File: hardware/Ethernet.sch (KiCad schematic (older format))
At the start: 29 parts, among them J2 RJ45-TRANSFO, U3 DP83848C, X1 50Mhz

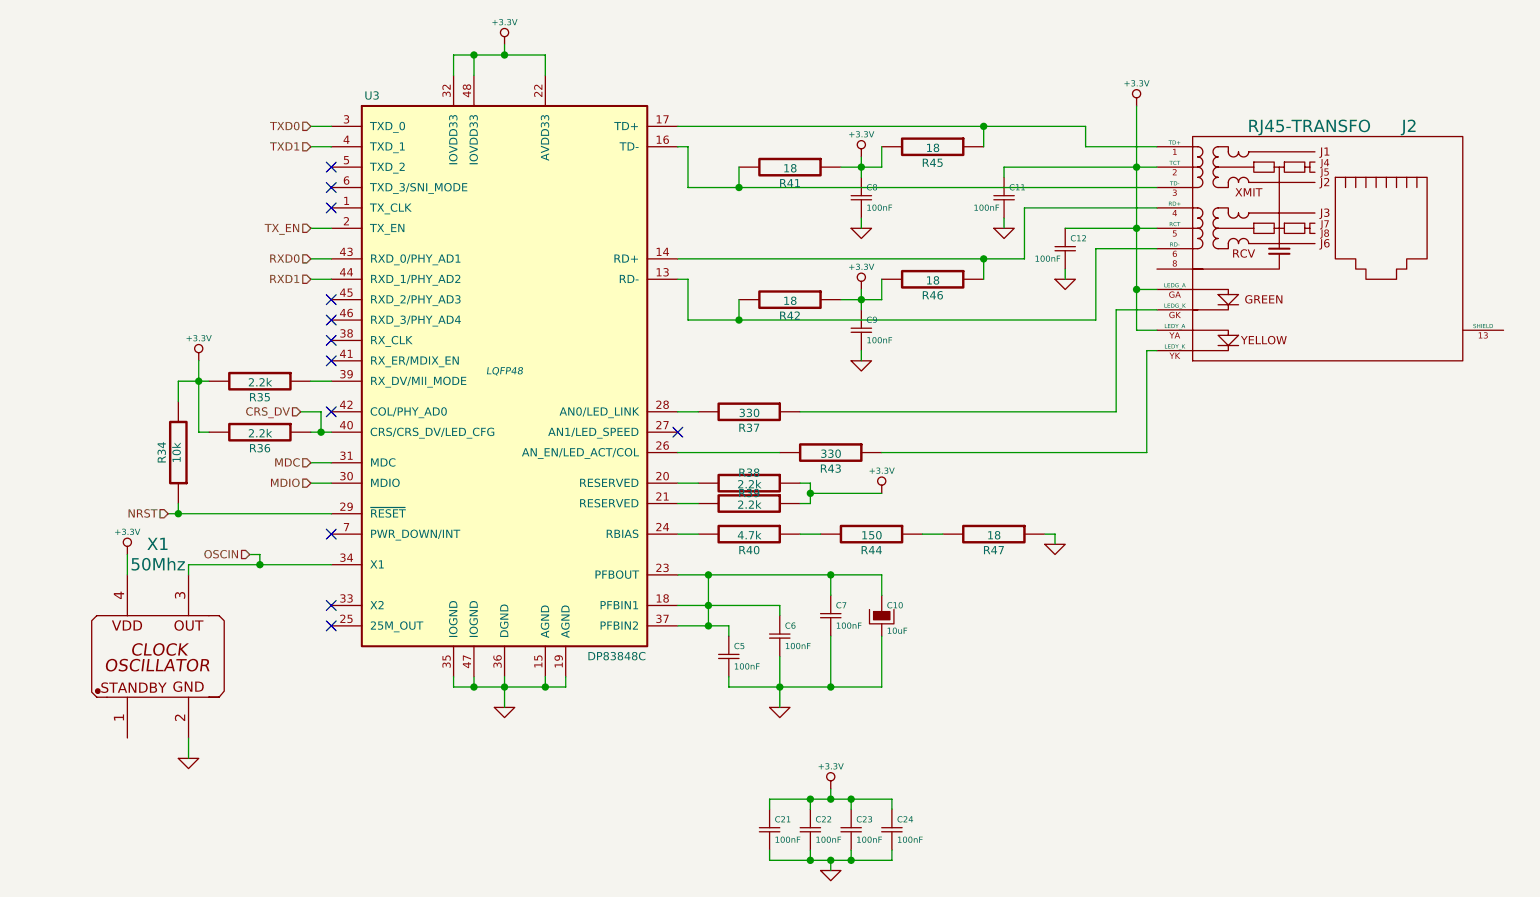
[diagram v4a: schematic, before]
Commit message: Terminado el Routeo de la Placa
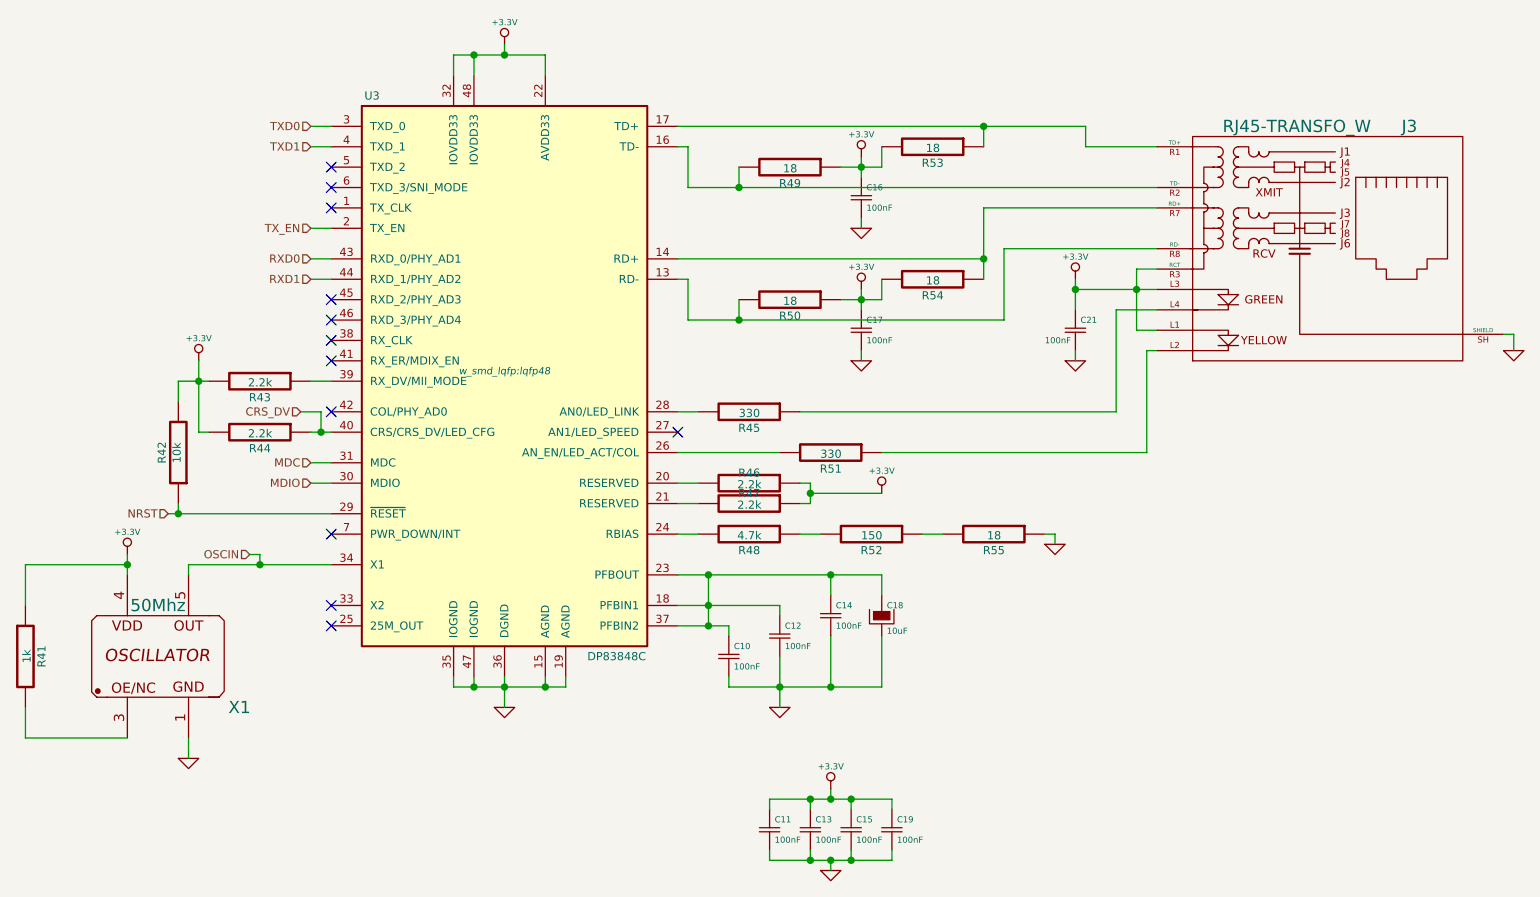
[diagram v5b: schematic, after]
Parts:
- removed C11: 100nF, Capacitors_SMD:c_1206, symbol Csmall
- removed J2: RJ45-TRANSFO, symbol RJ45-TRANSFO
- removed X1: 50Mhz, symbol OSCILLATOR-VDD-4
- added J3: RJ45-TRANSFO_W, w_Connectors:RJ45, symbol RJ45-TRANSFO_W
- added R41: 1k, Resistors_SMD:R_0805, symbol R
- added X1: 50Mhz, SMD_Packages:SOT-23-5, symbol OSCILLATOR-SOT23
- C10: renamed from C5; footprint Capacitors_SMD:c_1206 -> Capacitors_SMD:c_0805
- C11: renamed from C21; footprint Capacitors_SMD:c_1206 -> Capacitors_SMD:c_0805
- C12: renamed from C6; footprint Capacitors_SMD:c_1206 -> Capacitors_SMD:c_0805
- C13: renamed from C22; footprint Capacitors_SMD:c_1206 -> Capacitors_SMD:c_0805
- C14: renamed from C7; footprint Capacitors_SMD:c_1206 -> Capacitors_SMD:c_0805
- C15: renamed from C23; footprint Capacitors_SMD:c_1206 -> Capacitors_SMD:c_0805
- C16: renamed from C8; footprint Capacitors_SMD:c_1206 -> Capacitors_SMD:c_0805
- C17: renamed from C9; footprint Capacitors_SMD:c_1206 -> Capacitors_SMD:c_0805
- C19: renamed from C24; footprint Capacitors_SMD:c_1206 -> Capacitors_SMD:c_0805
- C21: renamed from C12; footprint Capacitors_SMD:c_1206 -> Capacitors_SMD:c_0805
- R42: renamed from R34; footprint Resistors_SMD:Resistor_SMD1206_ReflowWave -> Resistors_SMD:R_0805
- R43: renamed from R35; footprint Resistors_SMD:Resistor_SMD1206_ReflowWave -> Resistors_SMD:R_0805
- R44: renamed from R36; footprint Resistors_SMD:Resistor_SMD1206_ReflowWave -> Resistors_SMD:R_0805
- R45: renamed from R37; footprint Resistors_SMD:Resistor_SMD1206_ReflowWave -> Resistors_SMD:R_0805
- R46: renamed from R38; footprint Resistors_SMD:Resistor_SMD1206_ReflowWave -> Resistors_SMD:R_0805
- R47: renamed from R39; footprint Resistors_SMD:Resistor_SMD1206_ReflowWave -> Resistors_SMD:R_0805
- R48: renamed from R40; footprint Resistors_SMD:Resistor_SMD1206_ReflowWave -> Resistors_SMD:R_0805
- R49: renamed from R41; footprint Resistors_SMD:Resistor_SMD1206_ReflowWave -> Resistors_SMD:R_0805
- R50: renamed from R42; footprint Resistors_SMD:Resistor_SMD1206_ReflowWave -> Resistors_SMD:R_0805
- R51: renamed from R43; footprint Resistors_SMD:Resistor_SMD1206_ReflowWave -> Resistors_SMD:R_0805
- R52: renamed from R44; footprint Resistors_SMD:Resistor_SMD1206_ReflowWave -> Resistors_SMD:R_0805
- R53: renamed from R45; footprint Resistors_SMD:Resistor_SMD1206_ReflowWave -> Resistors_SMD:R_0805
- R54: renamed from R46; footprint Resistors_SMD:Resistor_SMD1206_ReflowWave -> Resistors_SMD:R_0805
- R55: renamed from R47; footprint Resistors_SMD:Resistor_SMD1206_ReflowWave -> Resistors_SMD:R_0805
- U3: footprint LQFP48 -> w_smd_lqfp:lqfp48
- renumbered C10 to C18
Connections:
- net +3.3V: now also J3.L1, J3.L3, J3.R3 (RCT), R41.1, X1.4 (VDD)
- net GND: now also J3.SH (SHIELD), X1.1 (GND)
- net OSCIN: now also X1.5 (OUT)
- net at R50.2, U3.13 (RD-): now also J3.R8 (RD-)
- net at R54.1, U3.14 (RD+): now also J3.R7 (RD+)
- net at R49.2, U3.16 (TD-): now also J3.R2 (TD-)
- net at R53.1, U3.17 (TD+): now also J3.R1 (TD+)
- net at R45.1: now also J3.L4
- net at R51.1: now also J3.L2
- new net: R41.2, X1.3 (STANDBY)
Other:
- moved on the sheet: C21

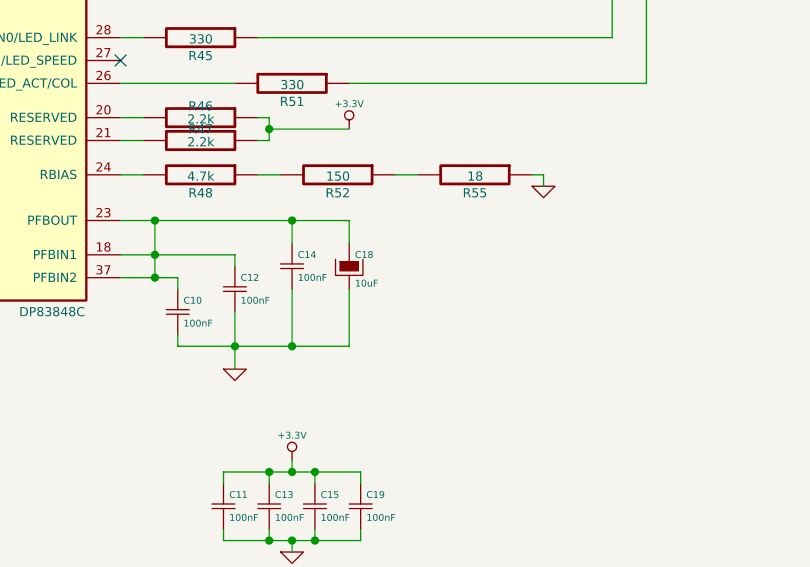
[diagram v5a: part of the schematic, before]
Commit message: Se reRouteo con clearance 12 en general
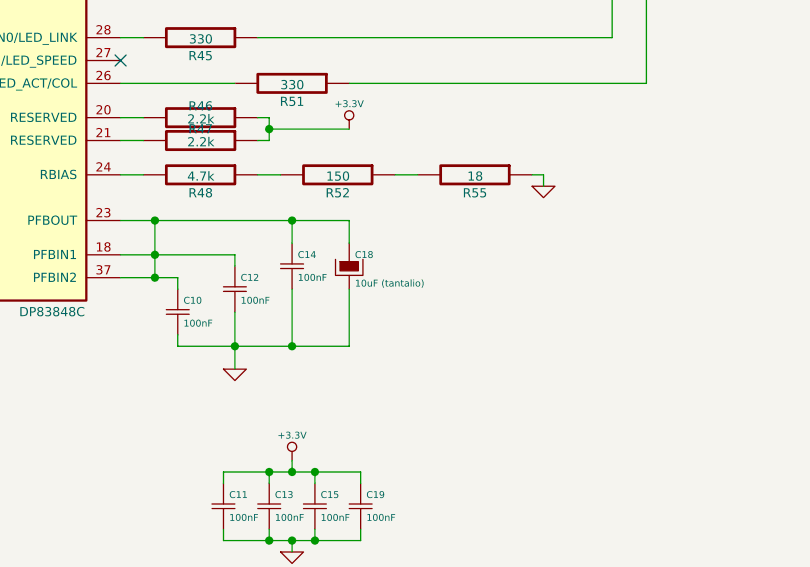
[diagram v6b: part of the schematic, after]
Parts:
- C18: value 10uF -> 10uF (tantalio); footprint Capacitors_ThroughHole:Capacitor5x11RM2.5 -> Capacitors_Tantalum_SMD:TantalC_SizeA_EIA-3216_HandSoldering
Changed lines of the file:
@@
 P 6350 4800
 F 0 "C18" H 6375 4850 30  0000 L CNN
-F 1 "10uF" H 6375 4725 30  0000 L CNN
-F 2 "Capacitors_ThroughHole:Capacitor5x11RM2.5" H 6350 4800 60  0001 C CNN
+F 1 "10uF (tantalio)" H 6375 4725 30  0000 L CNN
+F 2 "Capacitors_Tantalum_SMD:TantalC_SizeA_EIA-3216_HandSoldering" H 6350 4800 60  0001 C CNN
 F 3 "" H 6350 4800 60  0000 C CNN
 	1    6350 4800

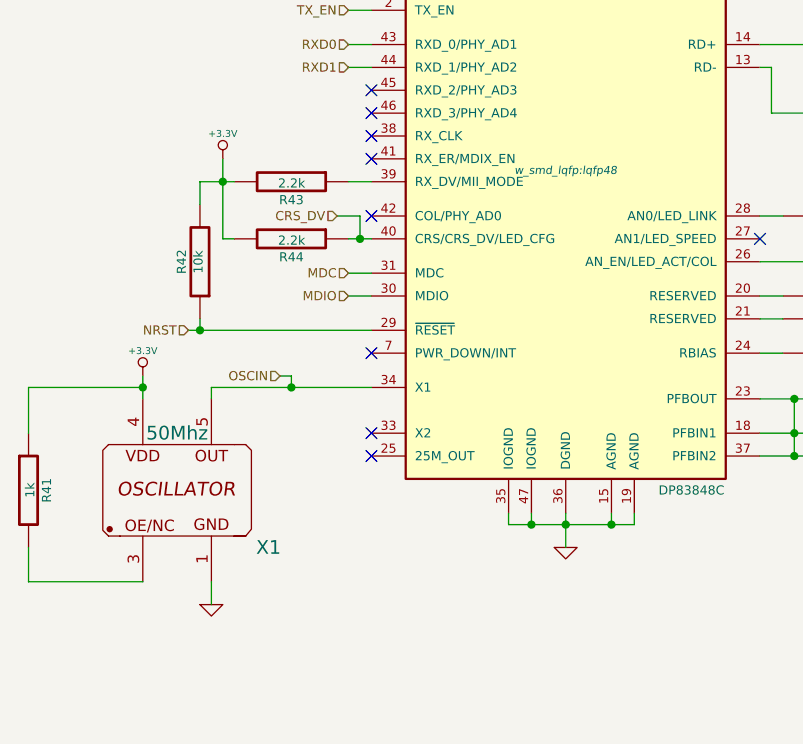
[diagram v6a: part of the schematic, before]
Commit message: Placa terminada, serigrafia verificada, logos agregados
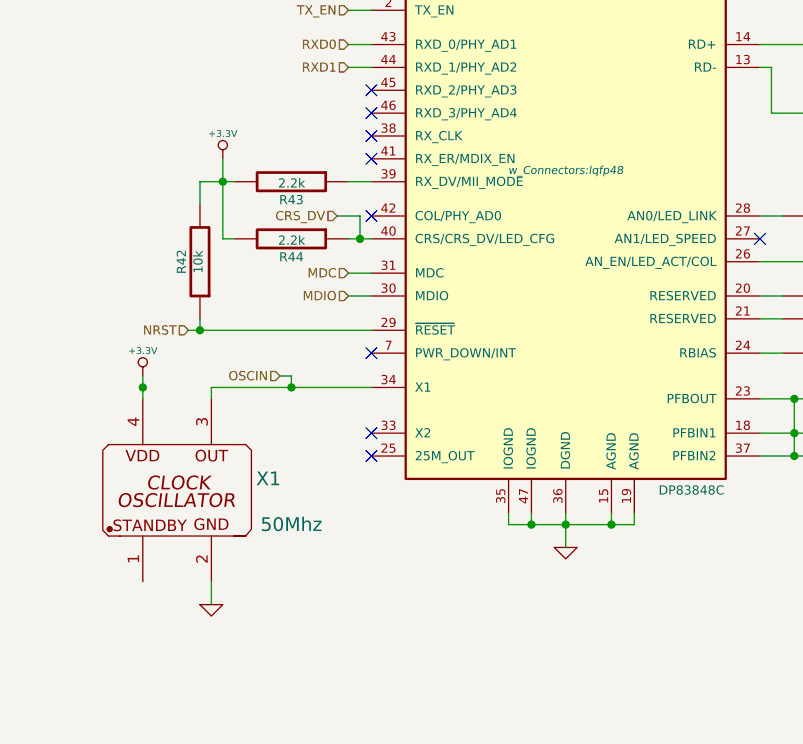
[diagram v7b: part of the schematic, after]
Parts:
- removed R41: 1k, Resistors_SMD:R_0805, symbol R
- removed X1: 50Mhz, SMD_Packages:SOT-23-5, symbol OSCILLATOR-SOT23
- added X1: 50Mhz, w_Connectors:crystal_fa128, symbol OSCILLATOR-VDD-4
- C10, C11, C12, C13, C14, C15, C16, C17, C19, C21: footprint Capacitors_SMD:c_0805 -> w_Connectors:c_0805
- U3: footprint w_smd_lqfp:lqfp48 -> w_Connectors:lqfp48
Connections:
- net +3.3V: now also X1.4 (VDD)
- net GND: now also X1.2 (GND)
- net OSCIN: now also X1.3 (OUT)
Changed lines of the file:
@@
 F 0 "U3" H 3850 4950 40  0000 C CNN
 F 1 "DP83848C" H 5050 2200 40  0000 C CNN
-F 2 "w_smd_lqfp:lqfp48" H 4500 3600 35  0000 C CIN
+F 2 "w_Connectors:lqfp48" H 4500 3600 35  0000 C CIN
 F 3 "" H 4500 3600 60  0000 C CNN
 	1    4500 3600
@@
 F 0 "C16" H 6275 2800 30  0000 L CNN
 F 1 "100nF" H 6275 2700 30  0000 L CNN
-F 2 "Capacitors_SMD:c_0805" H 6250 2750 60  0001 C CNN
+F 2 "w_Connectors:c_0805" H 6250 2750 60  0001 C CNN
 F 3 "" H 6250 2750 60  0000 C CNN
 	1    6250 2750
@@
 F 0 "C17" H 6275 3450 30  0000 L CNN
 F 1 "100nF" H 6275 3350 30  0000 L CNN
-F 2 "Capacitors_SMD:c_0805" H 6250 3400 60  0001 C CNN
+F 2 "w_Connectors:c_0805" H 6250 3400 60  0001 C CNN
 F 3 "" H 6250 3400 60  0000 C CNN
 	1    6250 3400
@@
 F 0 "C10" H 5625 5050 30  0000 L CNN
 F 1 "100nF" H 5625 4950 30  0000 L CNN
-F 2 "Capacitors_SMD:c_0805" H 5600 5000 60  0001 C CNN
+F 2 "w_Connectors:c_0805" H 5600 5000 60  0001 C CNN
 F 3 "" H 5600 5000 60  0000 C CNN
 	1    5600 5000
@@
 F 0 "C12" H 5875 4950 30  0000 L CNN
 F 1 "100nF" H 5875 4850 30  0000 L CNN
-F 2 "Capacitors_SMD:c_0805" H 5850 4900 60  0001 C CNN
+F 2 "w_Connectors:c_0805" H 5850 4900 60  0001 C CNN
 F 3 "" H 5850 4900 60  0000 C CNN
 	1    5850 4900
@@
 F 0 "C14" H 6125 4850 30  0000 L CNN
 F 1 "100nF" H 6125 4750 30  0000 L CNN
-F 2 "Capacitors_SMD:c_0805" H 6100 4800 60  0001 C CNN
+F 2 "w_Connectors:c_0805" H 6100 4800 60  0001 C CNN
 F 3 "" H 6100 4800 60  0000 C CNN
 	1    6100 4800
@@
 F 0 "C21" H 7325 3450 30  0000 L CNN
 F 1 "100nF" H 7150 3350 30  0000 L CNN
-F 2 "Capacitors_SMD:c_0805" H 7300 3400 60  0001 C CNN
+F 2 "w_Connectors:c_0805" H 7300 3400 60  0001 C CNN
 F 3 "" H 7300 3400 60  0000 C CNN
 	1    7300 3400
@@
 F 0 "C11" H 5825 5900 30  0000 L CNN
 F 1 "100nF" H 5825 5800 30  0000 L CNN
-F 2 "Capacitors_SMD:c_0805" H 5800 5850 60  0001 C CNN
+F 2 "w_Connectors:c_0805" H 5800 5850 60  0001 C CNN
 F 3 "" H 5800 5850 60  0000 C CNN
 	1    5800 5850
@@
 F 0 "C13" H 6025 5900 30  0000 L CNN
 F 1 "100nF" H 6025 5800 30  0000 L CNN
-F 2 "Capacitors_SMD:c_0805" H 6000 5850 60  0001 C CNN
+F 2 "w_Connectors:c_0805" H 6000 5850 60  0001 C CNN
 F 3 "" H 6000 5850 60  0000 C CNN
 	1    6000 5850
@@
 F 0 "C15" H 6225 5900 30  0000 L CNN
 F 1 "100nF" H 6225 5800 30  0000 L CNN
-F 2 "Capacitors_SMD:c_0805" H 6200 5850 60  0001 C CNN
+F 2 "w_Connectors:c_0805" H 6200 5850 60  0001 C CNN
 F 3 "" H 6200 5850 60  0000 C CNN
 	1    6200 5850
@@
 F 0 "C19" H 6425 5900 30  0000 L CNN
 F 1 "100nF" H 6425 5800 30  0000 L CNN
-F 2 "Capacitors_SMD:c_0805" H 6400 5850 60  0001 C CNN
+F 2 "w_Connectors:c_0805" H 6400 5850 60  0001 C CNN
 F 3 "" H 6400 5850 60  0000 C CNN
 	1    6400 5850
@@
 	6200 5950 6200 6000
 Connection ~ 6200 6000
-$Comp
-L OSCILLATOR-SOT23 X1
-U 1 1 53F235E3
-P 2800 5000
-F 0 "X1" H 3200 4750 60  0000 C CNN
-F 1 "50Mhz" H 2800 5250 60  0000 C CNN
-F 2 "SMD_Packages:SOT-23-5" H 2800 5000 40  0001 C CNN
-F 3 "" H 2800 5000 40  0000 C CNN
-	1    2800 5000
-	1    0    0    -1
-$EndComp
-$Comp
-L R R41
-U 1 1 53F23776
-P 2150 5000
-F 0 "R41" V 2230 5000 40  0000 C CNN
-F 1 "1k" V 2157 5001 40  0000 C CNN
-F 2 "Resistors_SMD:R_0805" V 2080 5000 30  0001 C CNN
-F 3 "" H 2150 5000 30  0000 C CNN
-	1    2150 5000
-	1    0    0    -1
-$EndComp
-Wire Wire Line
-	2650 5400 2150 5400
-Wire Wire Line
-	2150 5400 2150 5250
-Wire Wire Line
-	2150 4750 2150 4550
-Wire Wire Line
-	2150 4550 2650 4550
 Connection ~ 2650 4550
 $Comp
@@
 Wire Wire Line
 	9450 3420 9400 3420
+$Comp
+L OSCILLATOR-VDD-4 X1
+U 1 1 53F90C4F
+P 2800 5000
+F 0 "X1" H 3200 5050 60  0000 C CNN
+F 1 "50Mhz" H 3300 4850 60  0000 C CNN
+F 2 "w_Connectors:crystal_fa128" H 2800 5000 40  0001 C CNN
+F 3 "" H 2800 5000 40  0000 C CNN
+	1    2800 5000
+	1    0    0    -1
+$EndComp
 $EndSCHEMATC
